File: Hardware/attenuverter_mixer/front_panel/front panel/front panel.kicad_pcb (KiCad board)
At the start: 2 copper layers, 50.8 x 130.2 mm, 17 parts

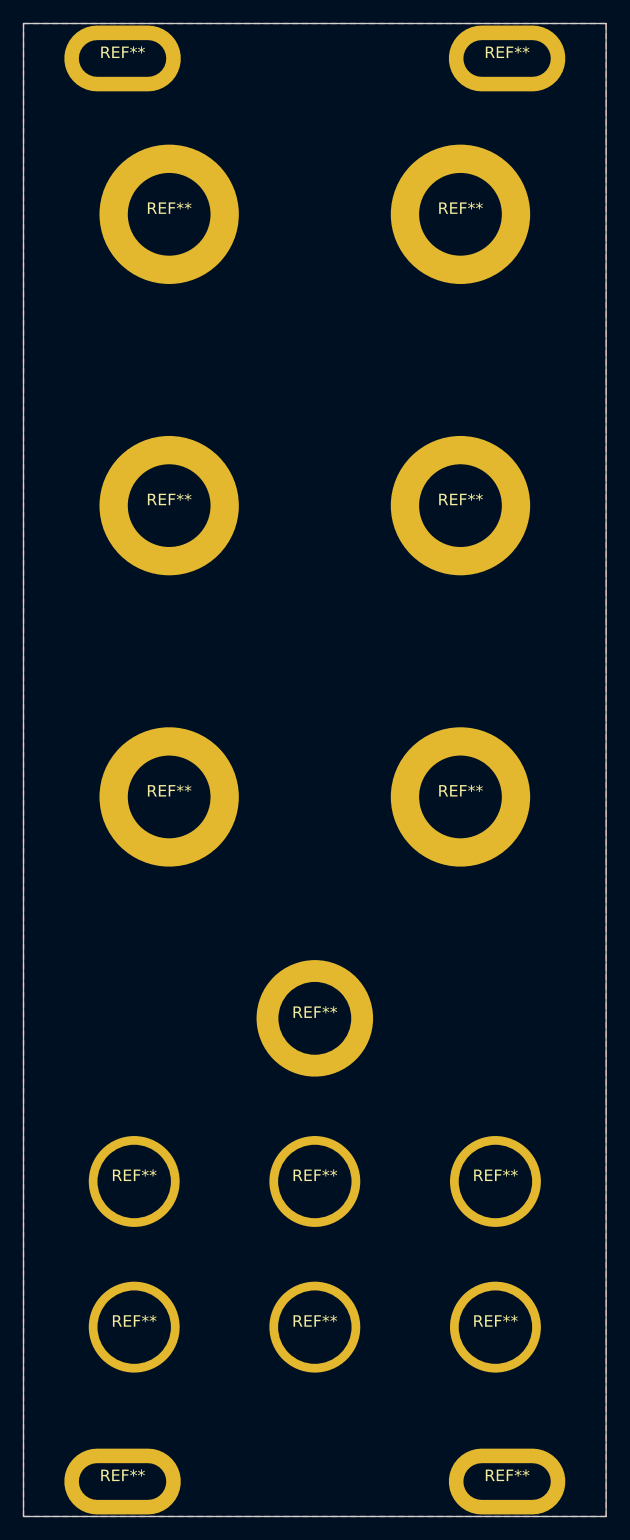
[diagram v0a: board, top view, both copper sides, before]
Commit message: created fabrication output
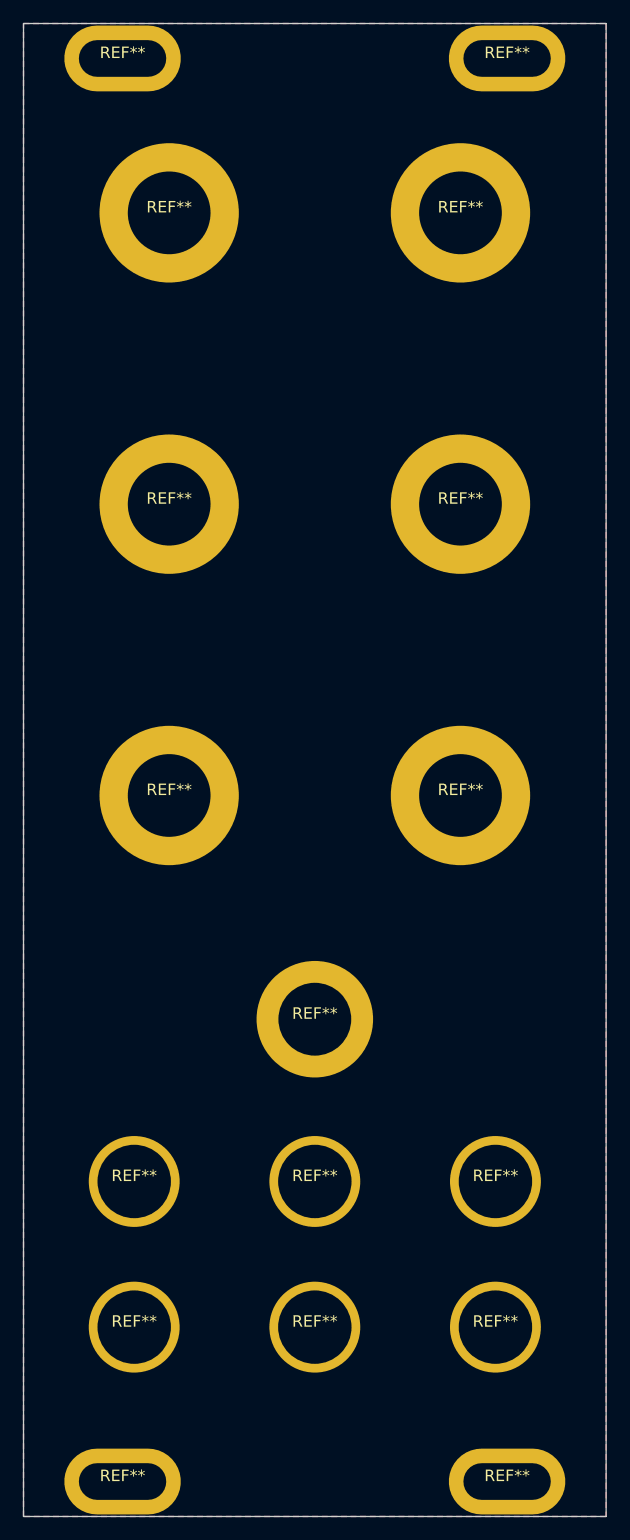
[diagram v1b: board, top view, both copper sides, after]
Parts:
- moved REF** 0.13 mm to (101.6, 92.6)
- moved REF** 0.13 mm to (127.0, 67.2)
- moved REF** 0.13 mm to (101.6, 118.0)
- moved REF** 0.13 mm to (101.6, 67.2)
- moved REF** 0.13 mm to (127.0, 118.0)
- moved REF** 0.13 mm to (127.0, 92.6)
- moved REF** 0.08 mm to (114.3, 137.5)
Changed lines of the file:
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@@
       (outputformat 1)
       (mirror false)
-      (drillshape 1)
+      (drillshape 0)
       (scaleselection 1)
-      (outputdirectory "")
+      (outputdirectory "gerbers/")
     )
   )
@@
   )
   (footprint "synthesis:PANEL_KNOB_SPECTRUM_SMALL" (layer "F.Cu")
-    (at 101.6 67.31)
+    (at 101.6 67.183)
     (attr through_hole)
     (fp_text reference "REF**" (at 0 -0.5 unlocked) (layer "F.SilkS")
@@
   )
   (footprint "synthesis:PANEL_KNOB_SPECTRUM_SMALL" (layer "F.Cu")
-    (at 127 118.11)
-    (attr through_hole)
-    (fp_text reference "REF**" (at 0 -0.5 unlocked) (layer "F.SilkS")
-        (effects (font (size 1 1) (thickness 0.1)))
-    )
-    (fp_text value "PANEL_KNOB_SPECTRUM_SMALL" (at 0 1 unlocked) (layer "F.Fab")
-        (effects (font (size 1 1) (thickness 0.15)))
-    )
-    (fp_text user "${REFERENCE}" (at 0 2.5 unlocked) (layer "F.Fab")
-        (effects (font (size 1 1) (thickness 0.15)))
-    )
-    (fp_rect (start -6.35 7.62) (end 6.35 11.43)
-      (stroke (width 0.1) (type default)) (fill none) (layer "Dwgs.User"))
-    (pad "1" thru_hole circle (at 0 0) (size 12.15 12.15) (drill 7.2136) (layers "*.Cu" "*.Mask")
-      (net 1 "GND") (zone_connect 2))
-  )
-  (footprint "synthesis:PANEL_KNOB_SPECTRUM_SMALL" (layer "F.Cu")
-    (at 127 92.71)
+    (at 127 117.983)
+    (attr through_hole)
+    (fp_text reference "REF**" (at 0 -0.5 unlocked) (layer "F.SilkS")
+        (effects (font (size 1 1) (thickness 0.1)))
+    )
+    (fp_text value "PANEL_KNOB_SPECTRUM_SMALL" (at 0 1 unlocked) (layer "F.Fab")
+        (effects (font (size 1 1) (thickness 0.15)))
+    )
+    (fp_text user "${REFERENCE}" (at 0 2.5 unlocked) (layer "F.Fab")
+        (effects (font (size 1 1) (thickness 0.15)))
+    )
+    (fp_rect (start -6.35 7.62) (end 6.35 11.43)
+      (stroke (width 0.1) (type default)) (fill none) (layer "Dwgs.User"))
+    (pad "1" thru_hole circle (at 0 0) (size 12.15 12.15) (drill 7.2136) (layers "*.Cu" "*.Mask")
+      (net 1 "GND") (zone_connect 2))
+  )
+  (footprint "synthesis:PANEL_KNOB_SPECTRUM_SMALL" (layer "F.Cu")
+    (at 127 92.583)
     (attr through_hole)
     (fp_text reference "REF**" (at 0 -0.5 unlocked) (layer "F.SilkS")
@@
   )
   (footprint "synthesis:PANEL_MINI_TOGGLE_DWB1" (layer "F.Cu")
-    (at 114.3 137.414)
+    (at 114.3 137.4902)
     (attr through_hole)
     (fp_text reference "REF**" (at 0 -0.5 unlocked) (layer "F.SilkS")
@@
   )
   (footprint "synthesis:PANEL_KNOB_SPECTRUM_SMALL" (layer "F.Cu")
-    (at 101.6 92.71)
+    (at 101.6 92.583)
     (attr through_hole)
     (fp_text reference "REF**" (at 0 -0.5 unlocked) (layer "F.SilkS")
@@
   )
   (footprint "synthesis:PANEL_KNOB_SPECTRUM_SMALL" (layer "F.Cu")
-    (at 127 67.31)
+    (at 127 67.183)
     (attr through_hole)
     (fp_text reference "REF**" (at 0 -0.5 unlocked) (layer "F.SilkS")
@@
   )
   (footprint "synthesis:PANEL_KNOB_SPECTRUM_SMALL" (layer "F.Cu")
-    (at 101.6 118.11)
+    (at 101.6 117.983)
     (attr through_hole)
     (fp_text reference "REF**" (at 0 -0.5 unlocked) (layer "F.SilkS")
@@
   (gr_rect (start 88.9 50.673) (end 139.7 180.848)
     (stroke (width 0.15) (type default)) (fill none) (layer "Dwgs.User"))
-  (gr_line (start 88.9 67.31) (end 139.7 67.31)
+  (gr_line (start 88.9 67.183) (end 139.7 67.183)
     (stroke (width 0.15) (type default)) (layer "Dwgs.User"))
   (gr_line (start 101.6 50.673) (end 101.6 180.848)
@@
   (gr_line (start 114.3 50.673) (end 114.3 180.848)
     (stroke (width 0.15) (type default)) (layer "Dwgs.User"))
-  (gr_line (start 88.9 118.11) (end 139.7 118.11)
-    (stroke (width 0.15) (type default)) (layer "Dwgs.User"))
-  (gr_line (start 88.9 137.414) (end 139.7 137.414)
+  (gr_line (start 88.9 117.983) (end 139.7 117.983)
+    (stroke (width 0.15) (type default)) (layer "Dwgs.User"))
+  (gr_line (start 88.9 137.4902) (end 139.7 137.4902)
     (stroke (width 0.15) (type default)) (layer "Dwgs.User"))
   (gr_line (start 98.552 151.638) (end 98.552 180.848)
     (stroke (width 0.15) (type default)) (layer "Dwgs.User"))
-  (gr_line (start 88.9 92.71) (end 139.7 92.71)
+  (gr_line (start 88.9 92.583) (end 139.7 92.583)
     (stroke (width 0.15) (type default)) (layer "Dwgs.User"))
   (gr_line (start 130.048 151.638) (end 130.048 180.848)

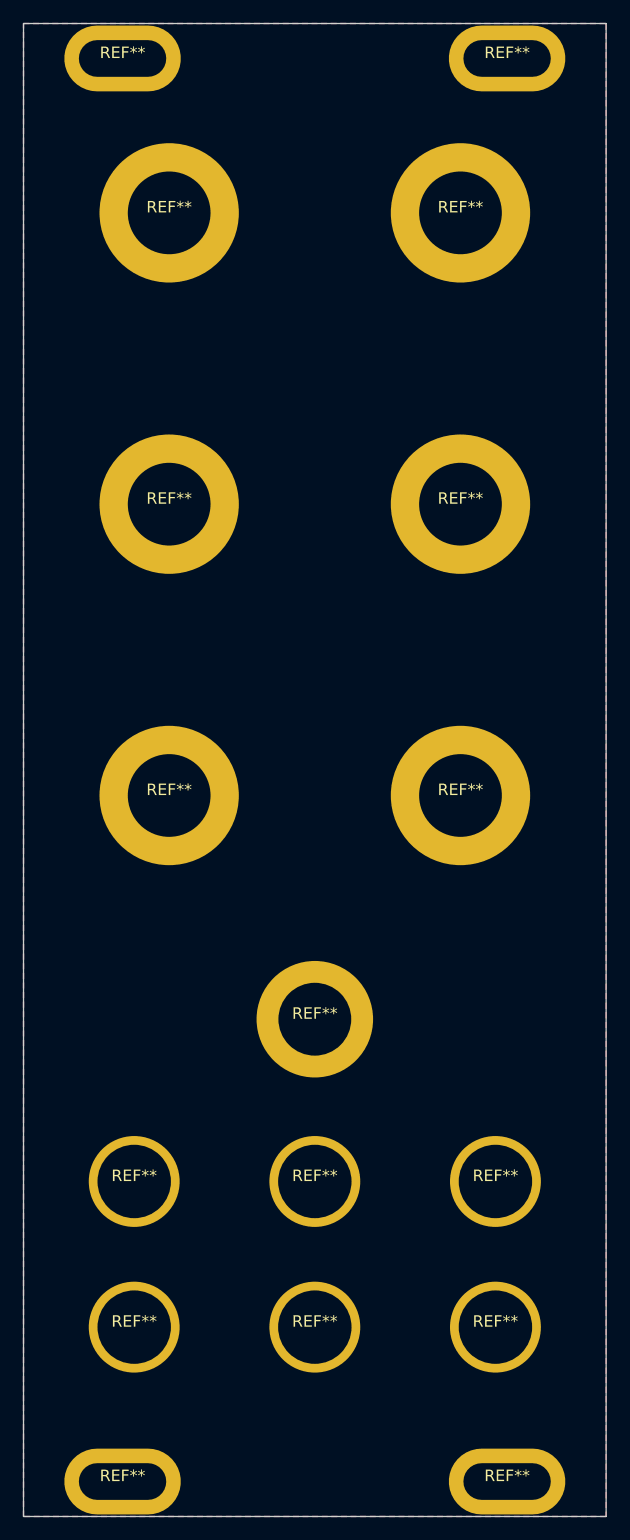
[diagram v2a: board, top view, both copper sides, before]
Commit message: fix rev A errors
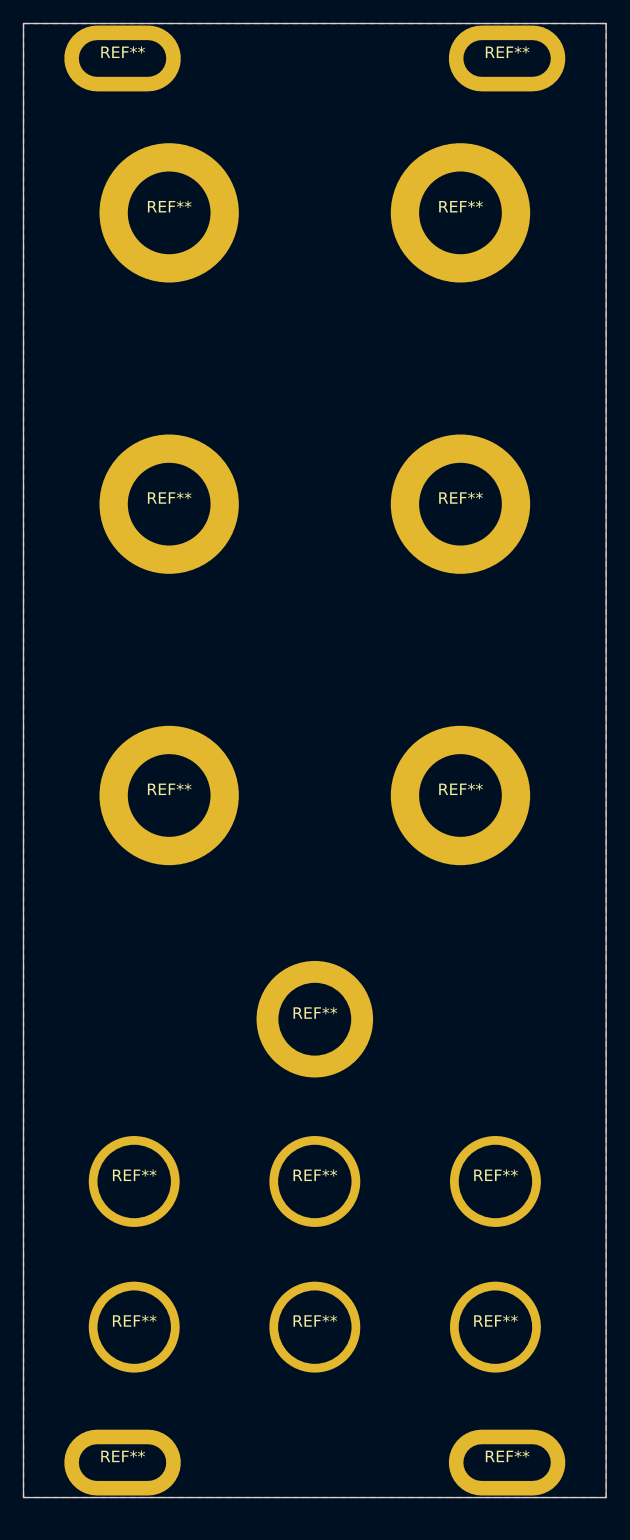
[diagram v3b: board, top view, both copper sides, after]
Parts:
- moved REF** 1.65 mm to (97.5, 176.1)
- moved REF** 1.65 mm to (131.1, 176.1)
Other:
- board size 50.8 x 130.2 mm -> 50.8 x 128.5 mm
- board text added: "Revision History Rev A: Original Proto Order Rev B: Correct Board Height"
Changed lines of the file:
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@@
 	(paper "A4")
 	(title_block
+		(rev "B")
 		(comment 4 "AISLER Project ID: RYDYGNWG")
 	)
@@
 	(footprint "synthesis:eurorack_mounting_hole"
 		(layer "F.Cu")
-		(at 131.064 177.8)
+		(at 131.064 176.149)
 		(property "Reference" "REF**"
 			(at 0 -0.5 0)
@@
 	(footprint "synthesis:eurorack_mounting_hole"
 		(layer "F.Cu")
-		(at 97.536 177.8)
+		(at 97.536 176.149)
 		(property "Reference" "REF**"
 			(at 0 -0.5 0)
@@
 		(layer "Dwgs.User")
 	)
+	(gr_line
+		(start 88.9 67.183)
+		(end 139.7 67.183)
+		(stroke
+			(width 0.15)
+			(type default)
+		)
+		(layer "Dwgs.User")
+	)
+	(gr_line
+		(start 101.6 50.673)
+		(end 101.6 180.848)
+		(stroke
+			(width 0.15)
+			(type default)
+		)
+		(layer "Dwgs.User")
+	)
+	(gr_line
+		(start 88.9 117.983)
+		(end 139.7 117.983)
+		(stroke
+			(width 0.15)
+			(type default)
+		)
+		(layer "Dwgs.User")
+	)
+	(gr_line
+		(start 88.9 137.4902)
+		(end 139.7 137.4902)
+		(stroke
+			(width 0.15)
+			(type default)
+		)
+		(layer "Dwgs.User")
+	)
+	(gr_line
+		(start 98.552 151.638)
+		(end 98.552 180.848)
+		(stroke
+			(width 0.15)
+			(type default)
+		)
+		(layer "Dwgs.User")
+	)
+	(gr_line
+		(start 88.9 92.583)
+		(end 139.7 92.583)
+		(stroke
+			(width 0.15)
+			(type default)
+		)
+		(layer "Dwgs.User")
+	)
+	(gr_line
+		(start 130.048 151.638)
+		(end 130.048 180.848)
+		(stroke
+			(width 0.15)
+			(type default)
+		)
+		(layer "Dwgs.User")
+	)
+	(gr_line
+		(start 88.9 164.338)
+		(end 139.7 164.338)
+		(stroke
+			(width 0.15)
+			(type default)
+		)
+		(layer "Dwgs.User")
+	)
+	(gr_line
+		(start 127 50.673)
+		(end 127 180.848)
+		(stroke
+			(width 0.15)
+			(type default)
+		)
+		(layer "Dwgs.User")
+	)
 	(gr_rect
 		(start 88.9 50.673)
-		(end 139.7 180.848)
-		(stroke
-			(width 0.15)
-			(type default)
-		)
-		(fill none)
-		(layer "Dwgs.User")
-	)
-	(gr_line
-		(start 88.9 67.183)
-		(end 139.7 67.183)
-		(stroke
-			(width 0.15)
-			(type default)
-		)
-		(layer "Dwgs.User")
-	)
-	(gr_line
-		(start 101.6 50.673)
-		(end 101.6 180.848)
-		(stroke
-			(width 0.15)
-			(type default)
-		)
-		(layer "Dwgs.User")
-	)
-	(gr_line
-		(start 114.3 50.673)
-		(end 114.3 180.848)
-		(stroke
-			(width 0.15)
-			(type default)
-		)
-		(layer "Dwgs.User")
-	)
-	(gr_line
-		(start 88.9 117.983)
-		(end 139.7 117.983)
-		(stroke
-			(width 0.15)
-			(type default)
-		)
-		(layer "Dwgs.User")
-	)
-	(gr_line
-		(start 88.9 137.4902)
-		(end 139.7 137.4902)
-		(stroke
-			(width 0.15)
-			(type default)
-		)
-		(layer "Dwgs.User")
-	)
-	(gr_line
-		(start 98.552 151.638)
-		(end 98.552 180.848)
-		(stroke
-			(width 0.15)
-			(type default)
-		)
-		(layer "Dwgs.User")
-	)
-	(gr_line
-		(start 88.9 92.583)
-		(end 139.7 92.583)
-		(stroke
-			(width 0.15)
-			(type default)
-		)
-		(layer "Dwgs.User")
-	)
-	(gr_line
-		(start 130.048 151.638)
-		(end 130.048 180.848)
-		(stroke
-			(width 0.15)
-			(type default)
-		)
-		(layer "Dwgs.User")
-	)
-	(gr_line
-		(start 88.9 164.338)
-		(end 139.7 164.338)
-		(stroke
-			(width 0.15)
-			(type default)
-		)
-		(layer "Dwgs.User")
-	)
-	(gr_line
-		(start 127 50.673)
-		(end 127 180.848)
-		(stroke
-			(width 0.15)
-			(type default)
-		)
-		(layer "Dwgs.User")
-	)
-	(gr_rect
-		(start 88.9 50.673)
-		(end 139.7 180.848)
+		(end 139.7 179.197)
 		(stroke
 			(width 0.1)
@@
 	)
 	(gr_text "ATTENUVERTER\nMIXER"
-		(at 114.3 176.784 0)
+		(at 114.3 175.26 0)
 		(layer "F.Mask")
 		(effects
@@
 				(thickness 0.2032)
 			)
+		)
+	)
+	(gr_text "Revision History\nRev A: Original Proto Order\nRev B: Correct Board Height"
+		(at 217.043 147.701 0)
+		(layer "User.1")
+		(effects
+			(font
+				(size 1 1)
+				(thickness 0.15)
+			)
+			(justify left bottom)
 		)
 	)
@@
 		(polygon
 			(pts
-				(xy 88.9 50.673) (xy 139.7 50.673) (xy 139.7 180.848) (xy 88.9 180.848)
+				(xy 88.9 50.673) (xy 139.7 50.673) (xy 139.7 179.197) (xy 88.9 179.197)
 			)
 		)
@@
 		(polygon
 			(pts
-				(xy 88.9 50.673) (xy 139.7 50.673) (xy 139.7 180.848) (xy 88.9 180.848)
-			)
-		)
+				(xy 88.9 50.673) (xy 139.7 50.673) (xy 139.7 179.197) (xy 88.9 179.197)
+			)
+		)
